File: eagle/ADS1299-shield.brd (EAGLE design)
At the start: 101.6 x 53.3 mm, 133 parts, among them IC1 ADS1299IPAG, IC2 TPS72325DBVT, IC3 TPS73225DBVT, IC5 24AA256UID, IC6 TPS604XXDBV, IC7 OPA376DBV, IC8 OPA376DBV, IC9 TXS0102DCTR, J8 Electrode Connector, U2 TXB0108PWR, U3 TXB0108PWR

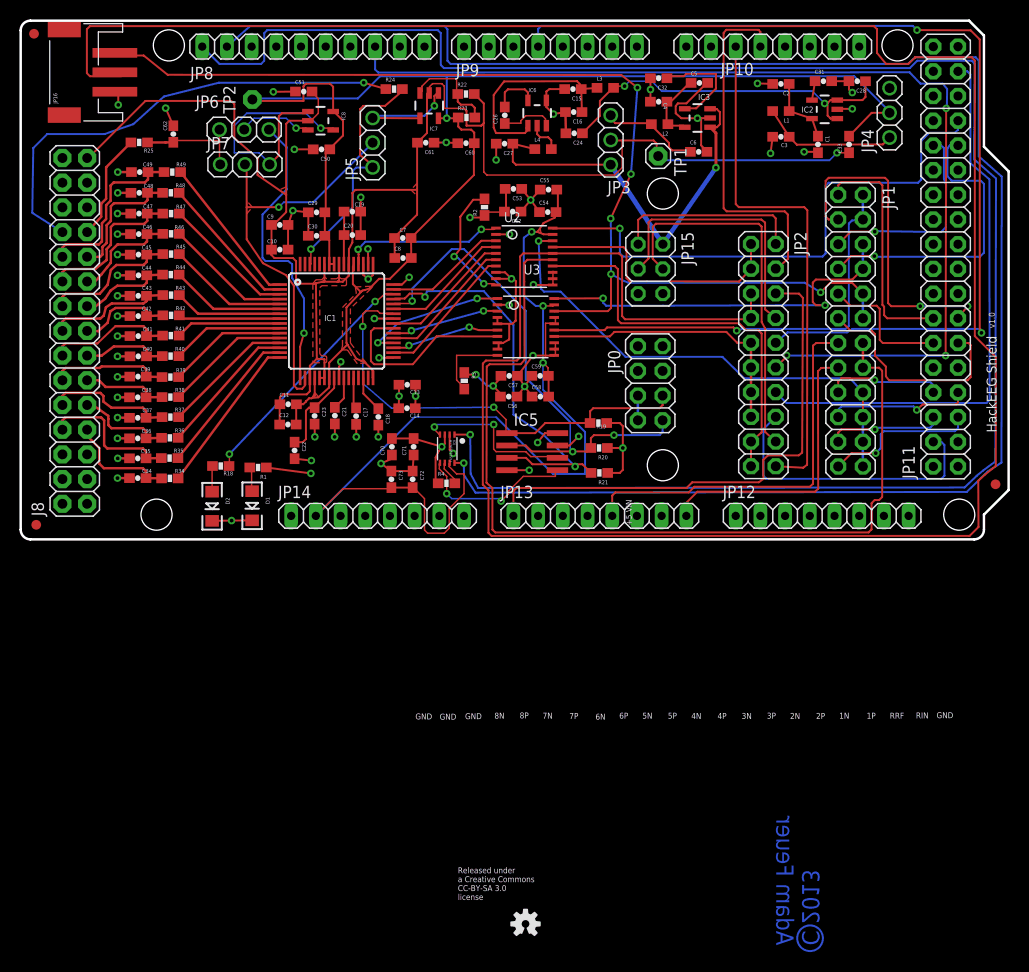
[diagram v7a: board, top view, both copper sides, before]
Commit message: many minor improvements - more mitering polygons, traces enlarged from 6mil to 8mil, clearances improved where possible
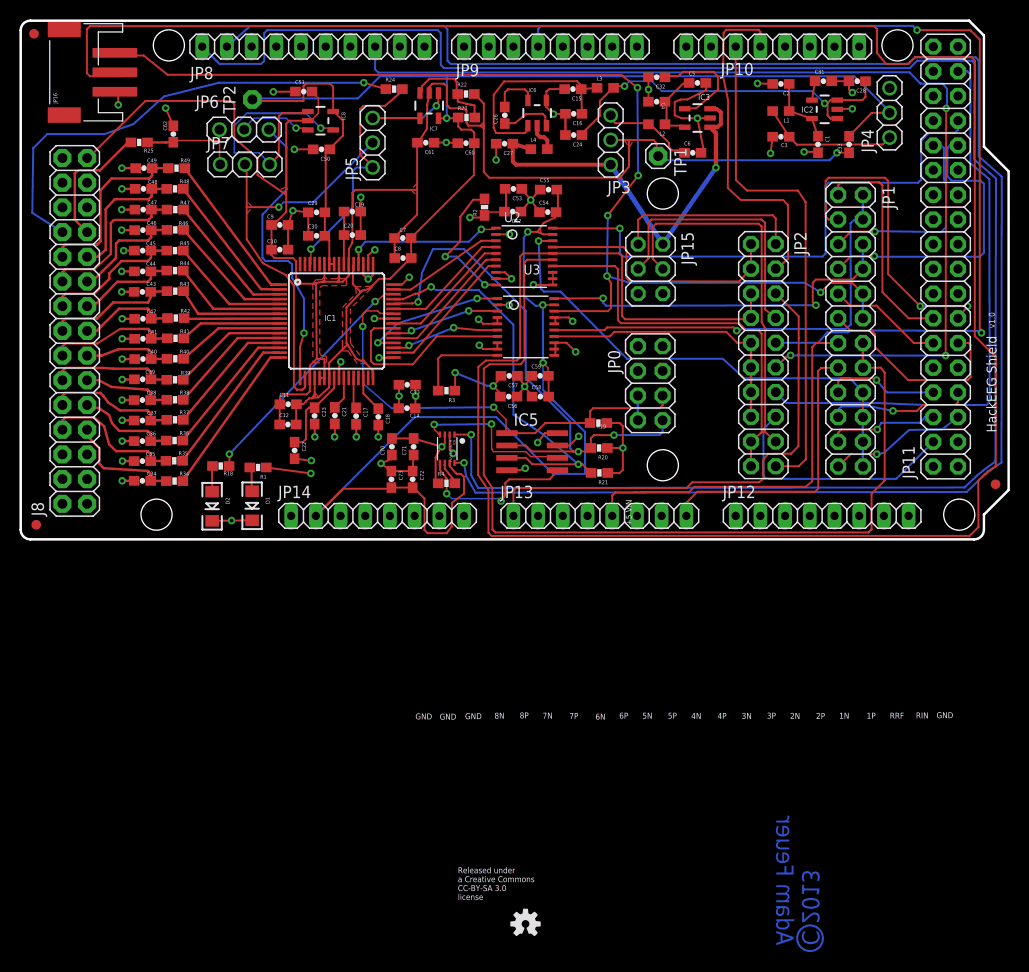
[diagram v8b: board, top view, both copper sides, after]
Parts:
- moved R3 2.09 mm to (43.9, 15.4), turned to 180 degrees
- moved C6 0.62 mm to (69.2, 39.9)
- moved C48 0.59 mm to (12.8, 36.2)
- moved R48 0.59 mm to (16.0, 36.2)
- moved C43 0.59 mm to (12.6, 25.6)
- moved R43 0.59 mm to (16.0, 25.7)
- moved C44 0.59 mm to (12.7, 27.7)
- moved C45 0.59 mm to (12.7, 29.8)
- moved C46 0.59 mm to (12.7, 31.9)
- moved R44 0.59 mm to (16.0, 27.8)
- moved C47 0.59 mm to (12.7, 34.0)
- moved C49 0.59 mm to (12.8, 38.3)
- moved R46 0.59 mm to (16.0, 32.0)
- moved R47 0.59 mm to (16.0, 34.0)
- moved R49 0.59 mm to (16.2, 38.3)
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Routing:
- net AGND: track 492.7 -> 508.4 mm, vias 53 -> 56
- net !ADC_CS_3: track 29.9 -> 25.8 mm
- net REF_ELEC_CON: track 11.1 -> 13.7 mm
- net USART1_SCK: track 53.9 -> 51.6 mm
- net DVDD: track 115.4 -> 117.5 mm
- net BOARD_ADDR_1: track 55.1 -> 57.1 mm
- net !ADS_RESET: track 40.1 -> 38.3 mm
- net ADC_START_1: track 13.8 -> 11.9 mm
- net !ADC_PWDN_0: track 34.3 -> 32.5 mm
- net ADC_DRDY_0: track 15.9 -> 14.2 mm
- net N$562: track 7.98 -> 9.53 mm
- net USART1_MOSI: track 53.3 -> 51.8 mm
- net N$561: track 13.2 -> 14.5 mm
- net !ADC_PWDN_1: track 24.4 -> 23.1 mm
- net ADC_START_0: track 23.0 -> 21.8 mm
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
